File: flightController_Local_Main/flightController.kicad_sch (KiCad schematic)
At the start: 29 parts, among them J1 U.FL-R-SMT10, J2 Conn_ARM_SWD, J3 USBC, U2 TESEO-LIV3F, U3 DPS368XTSA1, U4 STM32H723VETx, U6 TPS562201DDCR

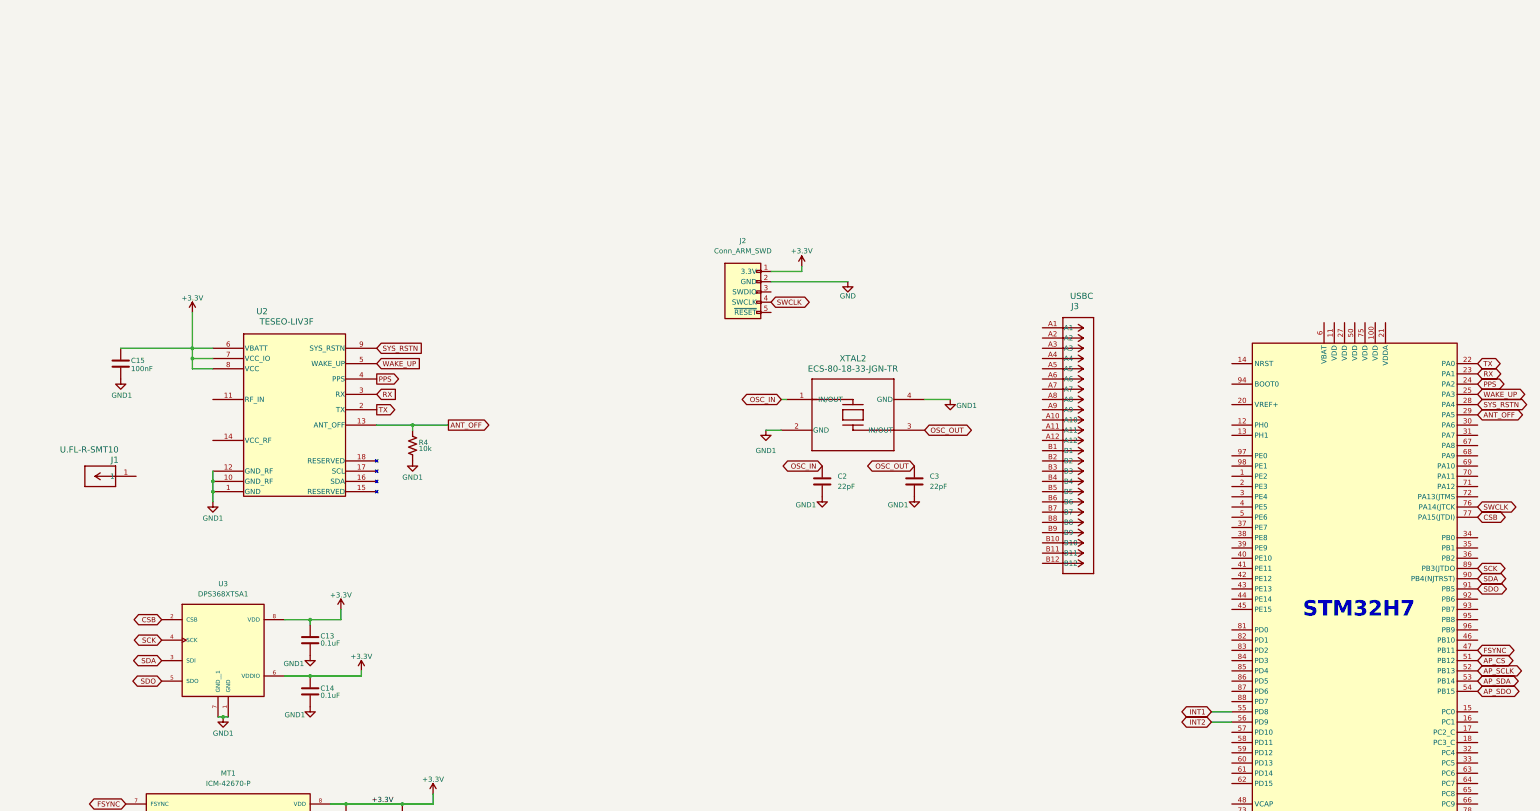
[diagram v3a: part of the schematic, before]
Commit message: Adding GPS passives and SWD
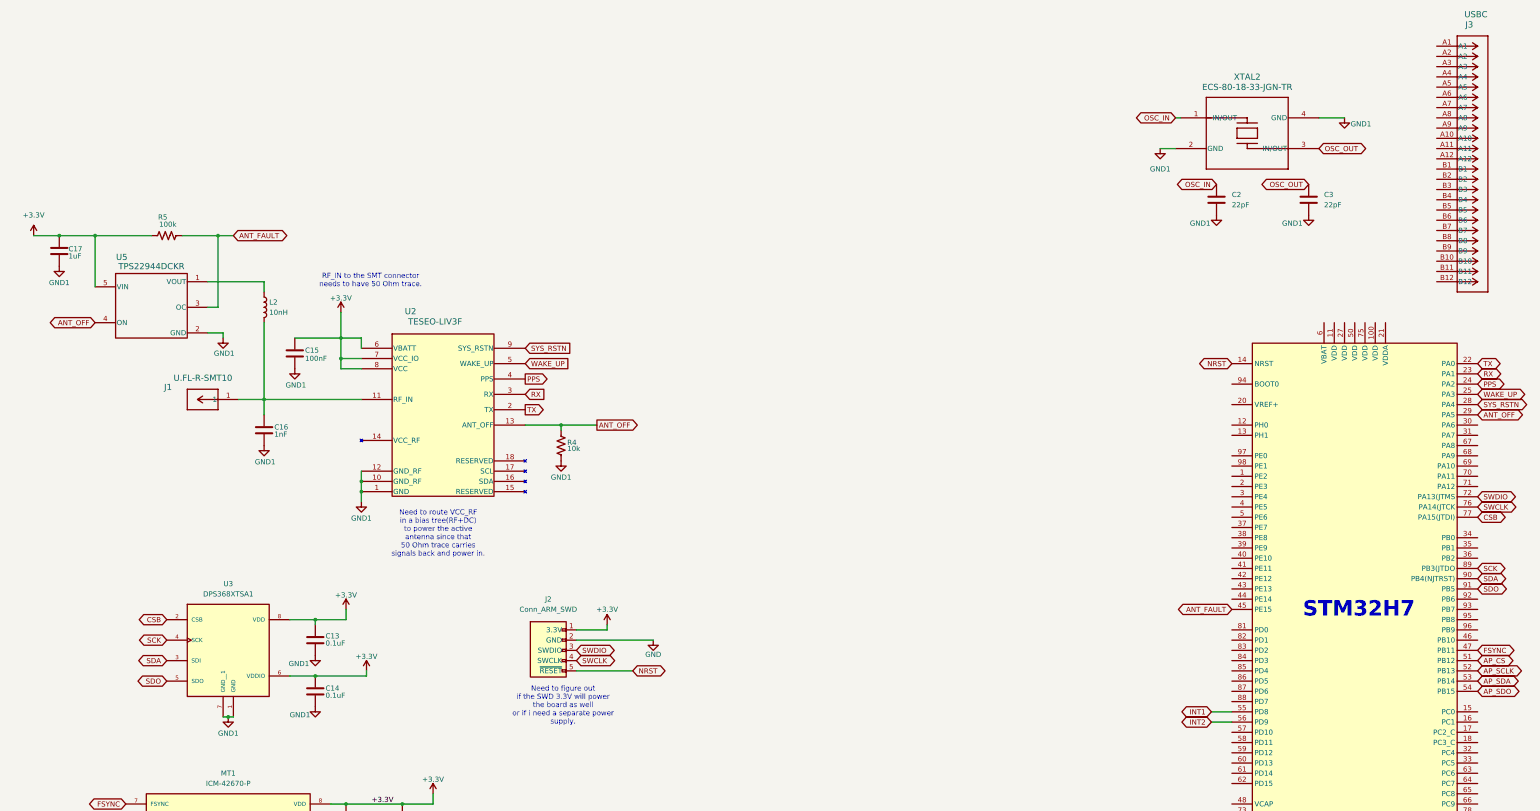
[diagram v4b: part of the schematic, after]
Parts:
- added C16: 1nF, symbol Device:C
- added C17: 1uF, symbol Device:C
- added L2: 10nH, symbol Device:L
- added R5: 100k, symbol Device:R_US
- added U5: TPS22944DCKR, DCK0005A_N, symbol TPS22944 (1):TPS22944DCKR
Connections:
- net +3.3V: now also C17.1, R5.2, U5.5 (VIN)
- net ANT_OFF: now also U5.4 (ON)
- net GND1: now also C16.2, C17.2, U5.2 (GND)
- net SWDIO: now reaches J2.3 (SWDIO)
- net SWDIO: now also U4.72 (PA13(JTMS)
- net NRST: now reaches J2.5 (~{RESET})
- net NRST: now also U4.14 (NRST)
- net ANT_FAULT: now reaches U4.45 (PE15)
- net ANT_FAULT: now also R5.1, U5.3 (OC)
- net at J1.1: now also U2.11 (RF_IN), C16.1, L2.2
- new net: L2.1, U5.1 (VOUT)
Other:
- note added: "Need to figure out if the SWD 3.3V will power the board as well or if i need a separate power supply."
- note added: "Need to route VCC_RF in a bias tree(RF+DC) to power the active antenna since that 50 Ohm trace carries signals back and power in."
- note added: "RF_IN to the SMT connector needs to have 50 Ohm trace."
- moved on the sheet: C13, C14, C15, C2, C3, J1, J2, J3, R4, U3, XTAL2

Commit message: Adding updates
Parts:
- added C18: 100nF, symbol Device:C
- added C19, C21: 4.7uF, symbol Device:C
- added C20: 1uF, symbol Device:C
- added D1, D2: ESD Protection, Library:ESD_6V (3), symbol Diode:ESD9B5.0ST5G
- added R6, R7: 5.1k, symbol Device:R_US
- added R8: 75k, symbol Device:R_US
- added R9: 100k, symbol Device:R_Small_US
- added U1: BD33IA5WEFJ-E2, HTSOP-J8_ROM, symbol 3.3V-LDO (1):BD33IA5WEFJ-E2
- added U7: MIC2004-0.5YM5-TR, Library:Current-Limiter-500mA (1), symbol Current-Limiter-500mA (1):MIC2004-0.5YM5-TR
- added U8, U9: LM66100DCKR, Library:Ideal_diode (2), symbol 3.3V-LDO (1):LM66100DCKR
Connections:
- net +3.3V: now also U8.6 (VOUT), U9.6 (VOUT); no longer C4.1, C5.1, C9.2, L1.1, R3.1
- net GND1: now also J3.A1, J3.A12, J3.B1, J3.B12, C18.2, C19.2, C20.2, C21.2, R6.2, R7.2, U1.3 (GND), U1.EPAD, U7.2 (GND), U8.2 (GND), U8.5 (ST), U9.2 (GND)
- net +5V_VBUS: now reaches U4.68 (PA9)
- net +5V_VBUS: now also J3.A4, J3.A9, J3.B4, J3.B9, C19.1, C20.1, R8.1, U1.5 (EN), U1.8 (VCC), U7.1 (VIN), U7.5 (VOUT)
- net D-: now reaches U4.70 (PA11)
- net D-: now also D2.1 (A1)
- net D+: now reaches U4.71 (PA12)
- net D+: now also D1.1 (A1)
- net at J3.A5: now also R6.1
- net at J3.A6: now also J3.B6, D1.2 (A2)
- net at J3.A7: now also J3.B7, D2.2 (A2)
- net at J3.B5: now also R7.1
- new net: R9.2, U8.3 (*CE), U9.5 (ST)
- new net: C18.1, R8.2, U7.3 (ENABLE)
- new net +3.3V_Batt: C4.1, C5.1, C9.2, L1.1, R3.1, U8.1 (VIN), U9.3 (*CE)
- new net 3.3V: C21.1, R9.1, U1.1 (VO), U1.2 (VO_S), U9.1 (VIN)
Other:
- note added: "3.3V Power + USBC"
- note added: "Enable is 1.2V R8 will lower the V to charge up C18. T(on)=RC(0.274) ~=2.06ms"
- note added: "Need to route D+/D- w/ ESD diodesand 22 ohm resistors USB C requires 90 0hm impedance paths < 20mm length"
- note added: "Needs to be wired to pin(1) GND at a single point"
- note added: "Needs to be wired to pin(2) SW close"
- note added: "Pull up resistor so U9 always has priority."
- note removed: "3.3V Power"
- moved on the sheet: C1, C10, C11, C12, C13, C14, C15, C16, C17, C2, C3, C4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
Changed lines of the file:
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@@
 	(generator "eeschema")
 	(generator_version "9.0")
-	(paper "A3")
+	(paper "A2")

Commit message: Adding the magnetometer and changing SPI pin outs
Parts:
- added C22: 220nF, symbol Device:C_Small
- added C23, C25: 100nF, symbol Device:C_Small
- added C26: 10uF, symbol Device:C_Small
- added U11: LIS2MDLTR, LIS2MDLTR:PQFN50P200X200X70-12N, symbol LIS2MDLTR:LIS2MDLTR
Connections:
- net +3.3V: now also C23.2, C25.1, C26.1, U11.10 (VDD_IO), U11.9 (VDD)
- net GND1: now also C22.2, C23.1, C25.2, C26.2, U11.6 (GND), U11.8 (GND__1)
- net SPI_1_CS_MAG: now reaches U4.34 (PB0)
- net SPI_1_CS_MAG: now also U11.3 (CS)
- net AP_CS renamed SPI_2_NSS
- net AP_SCLK renamed SPI_2_SCK
- net AP_SDA renamed SPI_2_MISO
- net AP_SDO renamed SPI_2_MOSI
- net CSB renamed SPI_1_NSS_IMU
- net SCK renamed SPI_1_SCK
- net SPI_1_SCK: now also U11.1 (SCL/SPC)
- net SDA renamed SPI_1_MISO
- net SPI_1_MISO: now also U11.4 (SDA/SDI/SDO)
- net SDO renamed SPI_1_MOSI
- net SPI_1_MOSI: now also U11.7 (INT/DRDY/SDO)
- new net: C22.1, U11.5 (C1)
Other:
- note added: "3.3V Buck Converter"
- note added: "Barometer"
- note added: "GPS (GNSS)"
- note added: "Gyroscope/Accelerometer"
- note added: "Magnetometer"
- note added: "Oscillator"
- note added: "SWD"
- note added: "USBC"
- moved on the sheet: C1, C10, C11, C12, C13, C14, C15, C16, C17, C18, C19, C2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
